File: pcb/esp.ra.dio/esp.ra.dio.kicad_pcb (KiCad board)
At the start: 2 copper layers, 75 x 28 mm, 24 parts, among them J1 A, J2 B, J3 C, J4 D, J5 START, J6 SELECT, J7 JOY, J8 BATTERY, J9 RADIO, SW1 OPTS, SW2 POWER, U1 RP2040 Tiny, U3 MIC5205-3.0YM5

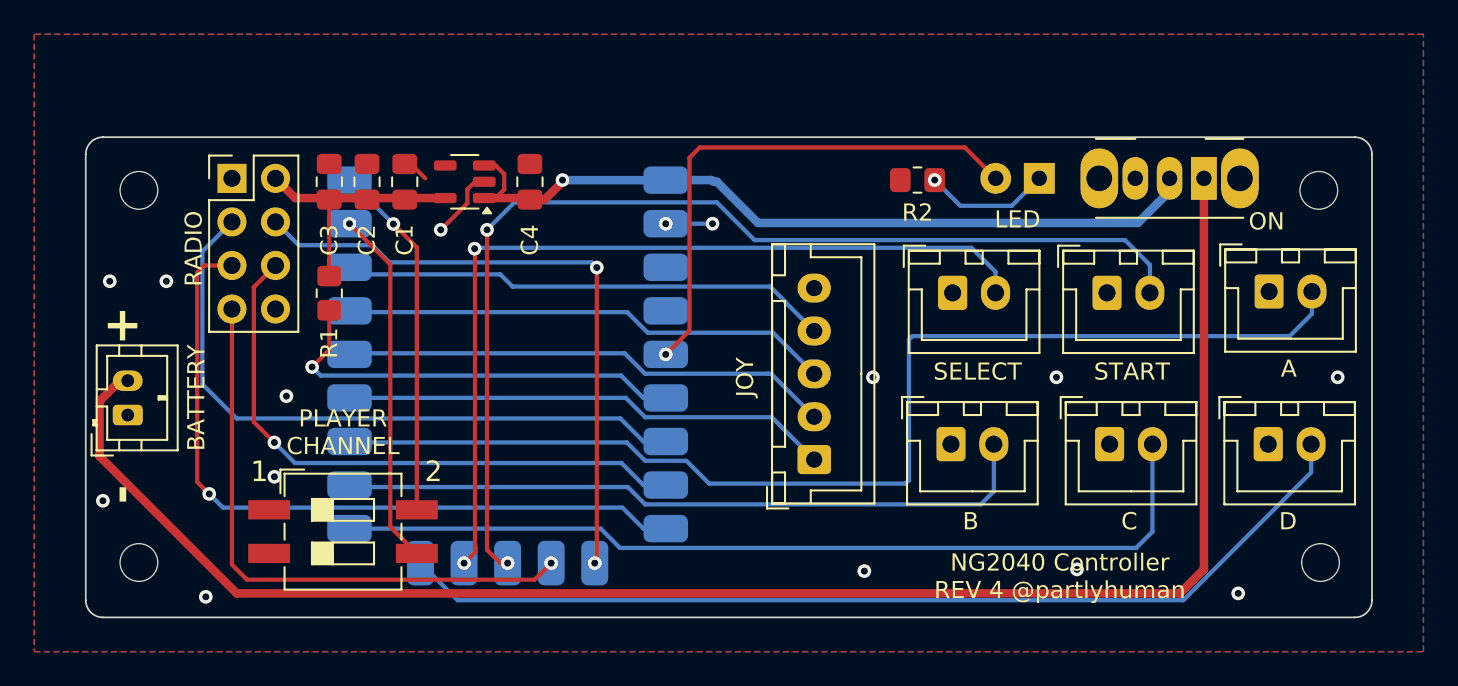
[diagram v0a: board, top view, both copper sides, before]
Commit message: super-mini symbol/footprint
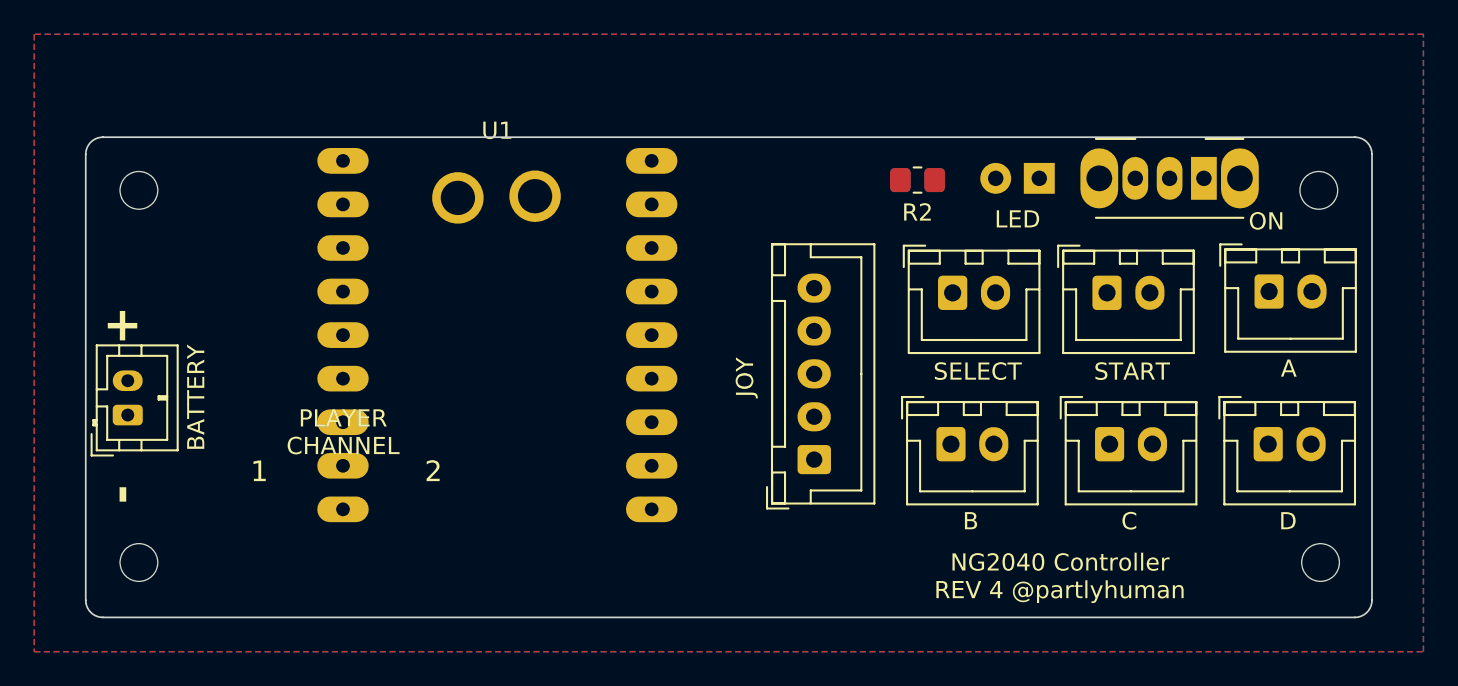
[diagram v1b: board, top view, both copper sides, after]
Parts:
- removed C1: 10uF, Capacitor_SMD:C_0805_2012Metric_Pad1.18x1.45mm_HandSolder
- removed C2: 0.1uF, Capacitor_SMD:C_0805_2012Metric_Pad1.18x1.45mm_HandSolder
- removed C3: 100nF, Capacitor_SMD:C_0805_2012Metric_Pad1.18x1.45mm_HandSolder
- removed C4: 1uF, Capacitor_SMD:C_0805_2012Metric_Pad1.18x1.45mm_HandSolder
- removed J9: RADIO, Connector_PinHeader_2.54mm:PinHeader_2x04_P2.54mm_Vertical
- removed R1: 10K, Resistor_SMD:R_0805_2012Metric_Pad1.20x1.40mm_HandSolder
- removed SW1: OPTS, Button_Switch_SMD:SW_DIP_SPSTx02_Slide_6.7x6.64mm_W8.61mm_P2.54mm_LowProfile
- removed U3: MIC5205-3.0YM5, Package_TO_SOT_SMD:SOT-23-5
- U1: value RP2040 Tiny -> ESP32-S3 Super Micro; footprint RP2040Zero:RP2040-Zero -> MCU_Espressif_ESP32_DevBoard:ESP32-S3-SuperMicro; moved to F.Cu
- moved U1 17.5 mm to (62.0, 61.5), turned to -90 degrees
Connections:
- SW2 pad 2: /VIN -> VCC
- U1 pad 1: /SET_PLAYER -> unconnected-(U1-TX-Pad1)
- U1 pad 10: /BD -> /D
- U1 pad 11: /SEL -> /C
- U1 pad 12: /STA -> /B
- U1 pad 13: /MISO -> /A
- U1 pad 14: /CS -> /STA
- U1 pad 15: /SCK -> /SEL
- U1 pad 16: /MOSI -> unconnected-(U1-3V3-Pad16)
- U1 pad 17: /CE -> GND
- U1 pad 18: Net-(U1-GP27) -> unconnected-(U1-5V-Pad18)
- U1 pad 19: /ACT_LED -> GND
- U1 pad 2: /SET_POWER -> unconnected-(U1-RX-Pad2)
- U1 pad 20: unconnected-(U1-GP29-Pad20) -> VCC
- U1 pad 3: /DL -> unconnected-(U1-GP1-Pad3)
- U1 pad 4: /DR -> unconnected-(U1-GP2-Pad4)
- U1 pad 5: /DD -> unconnected-(U1-GP3-Pad5)
- U1 pad 6: /DU -> /DL
- U1 pad 7: /BA -> /DR
- U1 pad 8: /BB -> /DD
- U1 pad 9: /BC -> /DU
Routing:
- net Net-(J8-Pin_2): track 96.4 -> 0.00 mm
- net /BA: track 67.3 -> 0.00 mm
- net /STA: track 62.6 -> 0.00 mm, vias 2 -> 0
- net /BD: track 57.6 -> 0.00 mm
- net /BC: track 52.8 -> 0.00 mm
- net /SEL: track 50.8 -> 0.00 mm, vias 2 -> 0
- net /VIN: track 46.7 -> 0.00 mm, vias 1 -> 0
- net /SCK: track 42.8 -> 0.00 mm, vias 1 -> 0
- net /BB: track 41.1 -> 0.00 mm
- net /CE: track 38.6 -> 0.00 mm
- net /CS: track 37.1 -> 0.00 mm, vias 2 -> 0
- net /MOSI: track 35.2 -> 0.00 mm, vias 1 -> 0
- net /MISO: track 34.3 -> 0.00 mm, vias 1 -> 0
- net /ACT_LED: track 30.9 -> 0.00 mm, vias 1 -> 0
- net /DD: track 28.7 -> 0.00 mm
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
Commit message: .
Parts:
- removed D1: LED, LED_THT:LED_D3.0mm_Horizontal_O1.27mm_Z6.0mm
- removed R2: 10K, Resistor_SMD:R_0805_2012Metric_Pad1.20x1.40mm_HandSolder
- removed SW2: POWER, Button_Switch_THT:SW_Slide_SPDT_Angled_CK_OS102011MA1Q
- J8: value BATTERY -> BAT
- U1: footprint MCU_Espressif_ESP32_DevBoard:ESP32-S3-SuperMicro -> MCU_Espressif_ESP32_DevBoard:ESP32-S3-SuperMicro_SMD_BATT
- moved U1 13.7 mm to (52.9, 51.2)
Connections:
- J8 pad 2: Net-(J8-Pin_2) -> /B+
- U1 pad 10: /D -> /BD
- U1 pad 11: /C -> /BC
- U1 pad 12: /B -> /BB
- U1 pad 13: /A -> /BA
- U1 pad 20: VCC -> /B+
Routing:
- net /BA: track 0.00 -> 55.0 mm
- net /BD: track 0.00 -> 43.9 mm
- net /BC: track 0.00 -> 36.5 mm
- net /STA: track 0.00 -> 32.9 mm, vias 0 -> 1
- net /DU: track 0.00 -> 32.6 mm, vias 0 -> 1
- net /B+: track 0.00 -> 30.8 mm
- net /DD: track 0.00 -> 29.8 mm, vias 0 -> 1
- net /DR: track 0.00 -> 28.7 mm, vias 0 -> 1
- net /DL: track 0.00 -> 28.7 mm, vias 0 -> 1
- net /BB: track 0.00 -> 27.6 mm
- net /SEL: track 0.00 -> 22.8 mm
- net GND: track 0.00 -> 3.11 mm, vias 0 -> 1
- removed copper zone on F.Cu, net GND
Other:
- board text removed: "1"
- board text removed: "2"
- board text removed: "ON"
- board text removed: "PLAYER CHANNEL"

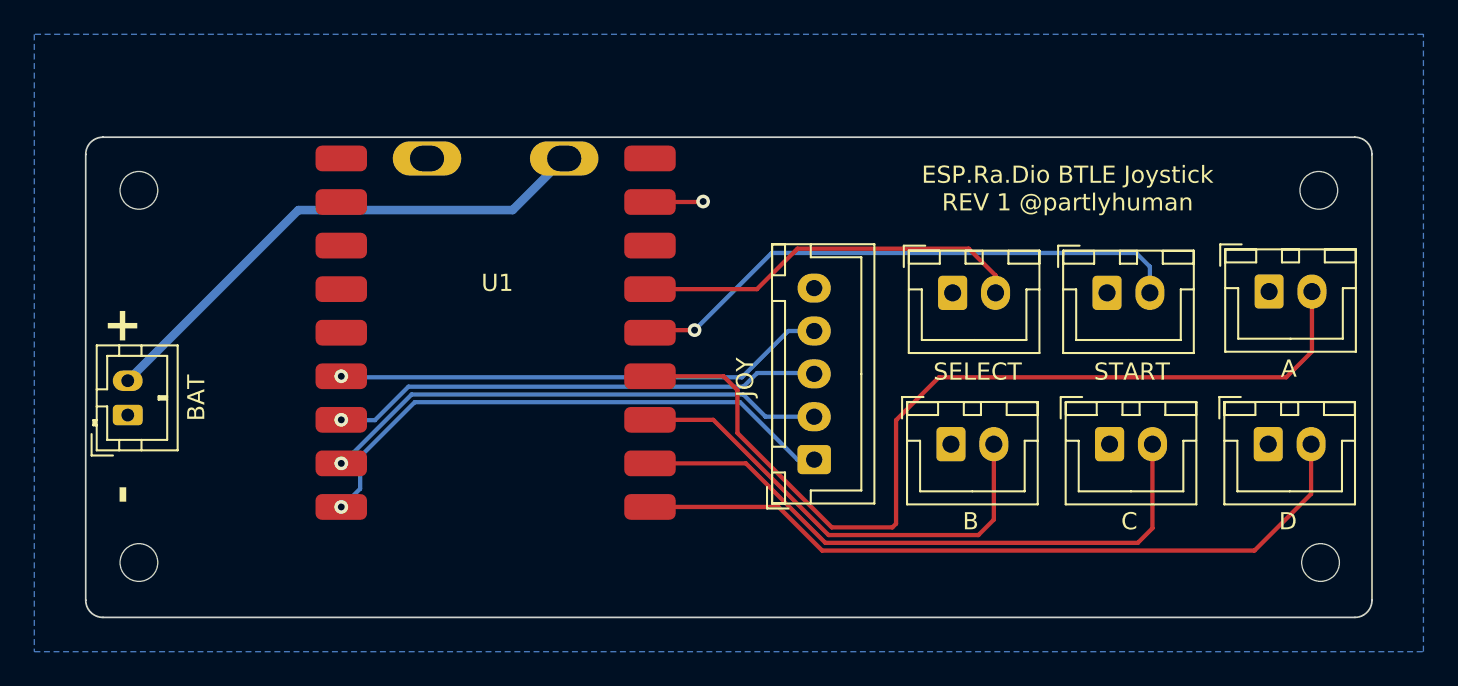
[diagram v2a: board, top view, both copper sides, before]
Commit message: Updated layout that keeps LED and switch
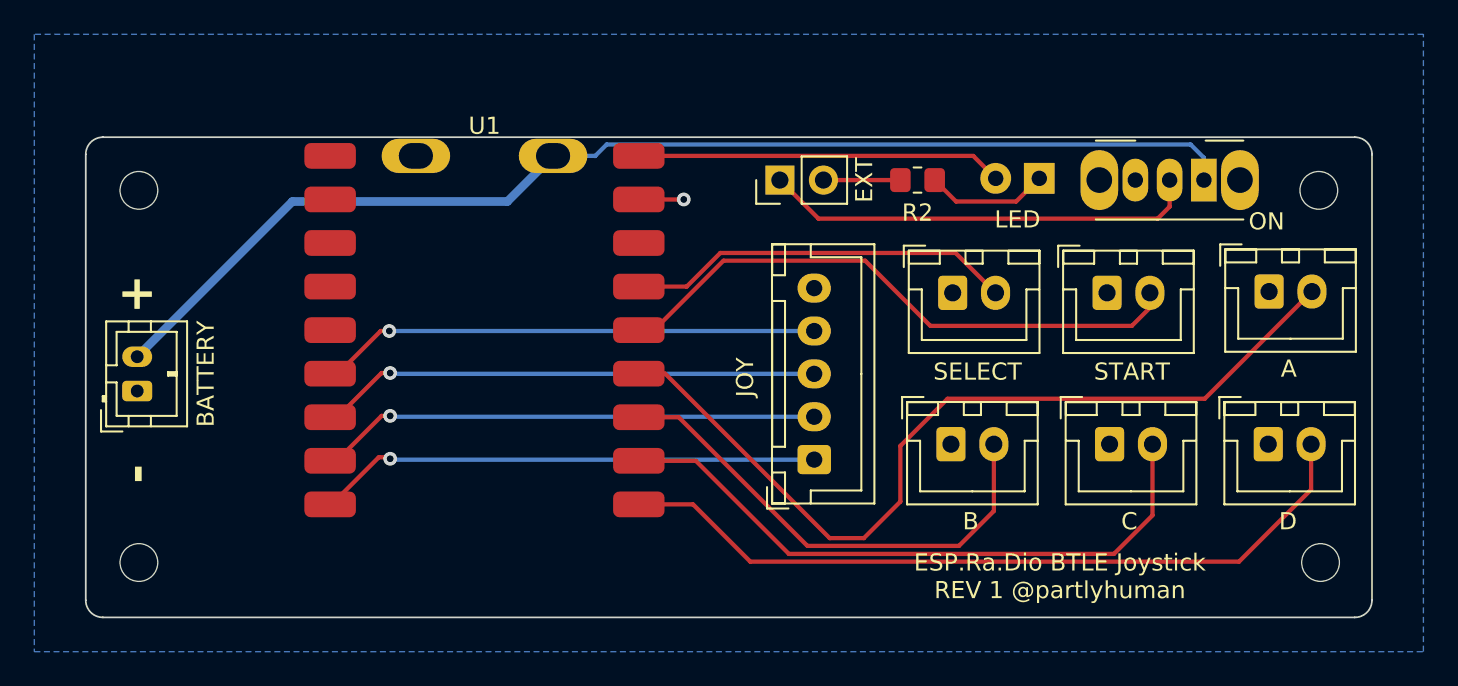
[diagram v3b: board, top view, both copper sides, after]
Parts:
- added D1: LED, LED_THT:LED_D3.0mm_Horizontal_O1.27mm_Z6.0mm, F.Cu at (93.6, 52.4)
- added J9: EXT, Connector_PinHeader_2.54mm:PinHeader_1x02_P2.54mm_Vertical, F.Cu at (78.5, 52.5)
- added R2: 10K, Resistor_SMD:R_0805_2012Metric_Pad1.20x1.40mm_HandSolder, F.Cu at (86.5, 52.5)
- added SW2: POWER, Button_Switch_THT:SW_Slide_SPDT_Angled_CK_OS102011MA1Q, F.Cu at (103.2, 52.5)
- J8: value BAT -> BATTERY
- moved J8 1.50 mm to (41.0, 64.8)
- moved U1 0.67 mm to (52.2, 51.1)
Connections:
- U1 pad 18: unconnected-(U1-5V-Pad18) -> /VBUS
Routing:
- net /B+: track 30.8 -> 69.2 mm
- net /LDO_CE: track 0.00 -> 25.5 mm
- net /VBUS: track 0.00 -> 21.4 mm
- net Net-(D1-K): track 0.00 -> 7.18 mm
- net /TP4054_CHRG: track 0.00 -> 4.48 mm
- net /BA: track 55.0 -> 51.1 mm
- net /DU: track 32.6 -> 29.4 mm
- net /STA: track 32.9 -> 34.4 mm, vias 1 -> 0
- net /BD: track 43.9 -> 45.0 mm
- net /BB: track 27.6 -> 28.5 mm
- net /BC: track 36.5 -> 37.3 mm
- net /DR: track 28.7 -> 29.3 mm
- net /DL: track 28.7 -> 29.3 mm
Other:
- board text added: "ON"

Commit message: Enough dev boards, redo with WROOM
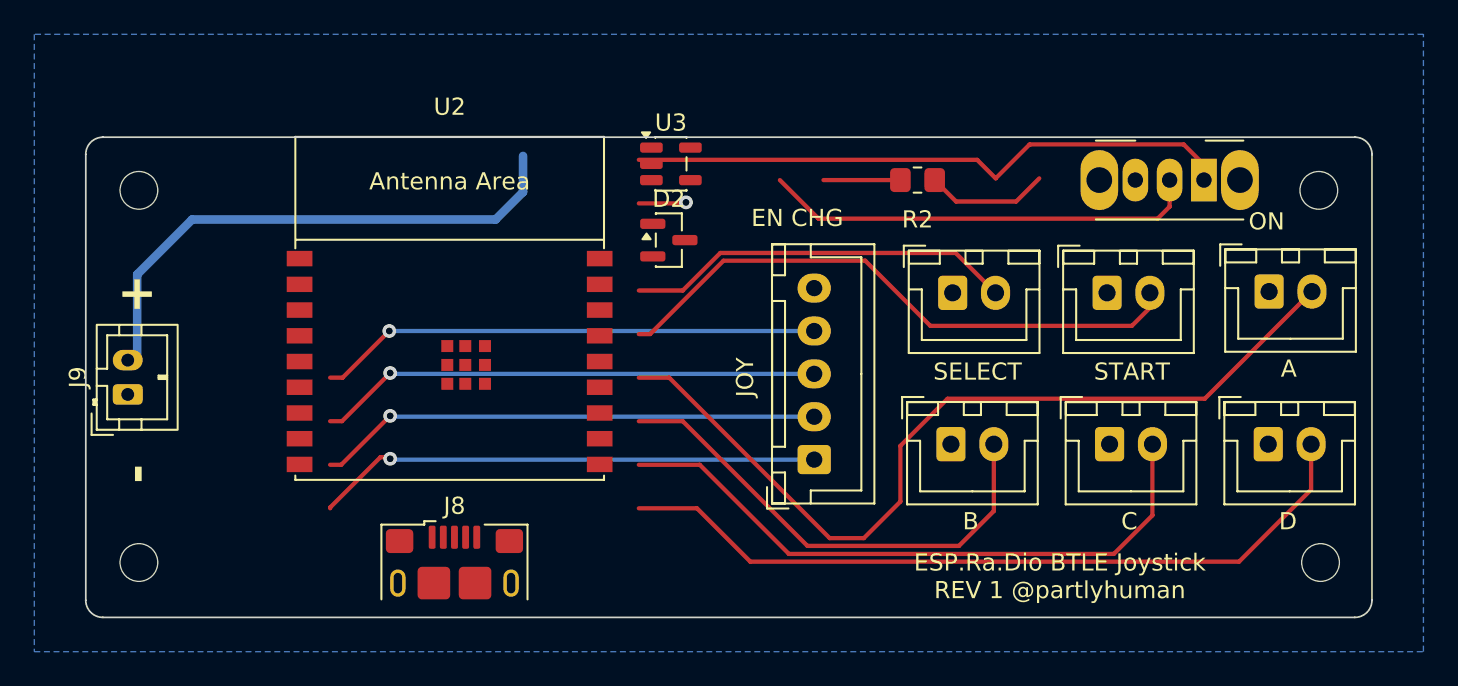
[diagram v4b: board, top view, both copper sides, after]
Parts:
- removed D1: LED, LED_THT:LED_D3.0mm_Horizontal_O1.27mm_Z6.0mm
- removed U1: ESP32-S3 Super Micro, MCU_Espressif_ESP32_DevBoard:ESP32-S3-SuperMicro_SMD_BATT
- added D2: BAT54C, Package_TO_SOT_SMD:SOT-23, F.Cu at (72.0, 56.0)
- added U2: ESP32-C3-WROOM-02, PCM_Espressif:ESP32-C3-WROOM-02, F.Cu at (59.2, 63.0)
- added U3: TLV75533PDBV, Package_TO_SOT_SMD:SOT-23-5, F.Cu at (72.1, 51.6)
- H1, H2, H3, H4: value MountingHole_2.2mm_M2 -> MountingHole
- J8: value BATTERY -> USB_B_Micro; footprint Connector_JST:JST_PH_B2B-PH-K_1x02_P2.00mm_Vertical -> Connector_USB:USB_Micro-B_Amphenol_10118193-0001LF_Horizontal
- J9: value EXT -> BATTERY; footprint Connector_PinHeader_2.54mm:PinHeader_1x02_P2.54mm_Vertical -> Connector_JST:JST_PH_B2B-PH-K_1x02_P2.00mm_Vertical
- R2: value 10K -> 0R
- moved J9 40.0 mm to (40.5, 65.0)
- moved J8 21.6 mm to (59.5, 76.0), turned to 0 degrees
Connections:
- J8 pad 1: GND -> /VBUS
- J8 pad 2: /B+ -> /USB_DN
- J9 pad 1: /LDO_CE -> GND
- J9 pad 2: /TP4054_CHRG -> /VBAT
- R2 pad 2: /TP4054_CHRG -> /USB_DP
- SW2 pad 1: /B+ -> GND
- SW2 pad 2: /LDO_CE -> Net-(SW2-B)
- SW2 pad 3: GND -> Net-(SW2-C)
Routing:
- net /B+: track 69.2 -> 0.00 mm
- net GND: track 2.62 -> 38.4 mm
- net /VBAT: track 0.00 -> 31.6 mm
- net Net-(SW2-B): track 0.00 -> 25.5 mm
- net /LDO_CE: track 25.5 -> 0.00 mm
- net /VBUS: track 21.4 -> 0.00 mm
- net /USB_DP: track 0.00 -> 4.48 mm
- net /TP4054_CHRG: track 4.48 -> 0.00 mm
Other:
- board text added: "EN CHG"

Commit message: Routing checkpoint
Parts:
- added C1: 10uF, Capacitor_SMD:C_0805_2012Metric_Pad1.18x1.45mm_HandSolder, F.Cu at (51.8, 61.0)
- added C2: 0.1uF, Capacitor_SMD:C_0805_2012Metric_Pad1.18x1.45mm_HandSolder, F.Cu at (54.2, 61.0)
- added C3: 1uF, Capacitor_SMD:C_0805_2012Metric_Pad1.18x1.45mm_HandSolder, F.Cu at (58.5, 74.5)
- added J10: UART, Connector_PinHeader_2.54mm:PinHeader_1x04_P2.54mm_Vertical, F.Cu at (80.0, 53.0)
- added R1: 0R, Resistor_SMD:R_0805_2012Metric_Pad1.20x1.40mm_HandSolder, F.Cu at (54.2, 66.0)
- added R3: 10K, Resistor_SMD:R_0805_2012Metric_Pad1.20x1.40mm_HandSolder, F.Cu at (61.5, 74.5)
- added SW1: RESET, Button_Switch_SMD:SW_SPST_PTS810, F.Cu at (67.0, 74.5)
- added SW3: BOOT, Button_Switch_SMD:SW_SPST_PTS810, F.Cu at (73.5, 74.5)
- J8: footprint Connector_USB:USB_Micro-B_Amphenol_10118193-0001LF_Horizontal -> Connector_USB:USB_Micro-AB_Molex_47590-0001
- moved SW2 50.7 mm to (52.5, 52.5)
- moved R2 37.3 mm to (51.8, 66.0), turned to -90 degrees
- moved U3 28.8 mm to (47.2, 66.0), turned to -90 degrees
- moved D2 25.2 mm to (47.2, 61.0), turned to 90 degrees
- moved J8 8.80 mm to (50.8, 76.9)
- moved U2 7.30 mm to (66.5, 63.5)
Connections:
- net Net-(SW2-B) renamed /VIN
- net Net-(SW2-C) renamed /VBATBUS
- D2 pad 1: /VBUS -> /VBAT
- D2 pad 2: /VBAT -> /VBUS
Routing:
- net /BA: track 51.0 -> 0.00 mm
- net /BD: track 44.9 -> 0.00 mm
- net /BC: track 37.2 -> 0.00 mm
- net /STA: track 34.5 -> 0.00 mm
- net GND: track 38.4 -> 4.27 mm, vias 1 -> 0
- net /DU: track 29.5 -> 0.00 mm, vias 1 -> 0
- net /DD: track 29.4 -> 0.00 mm, vias 1 -> 0
- net /DR: track 29.4 -> 0.00 mm, vias 1 -> 0
- net /DL: track 29.4 -> 0.00 mm, vias 1 -> 0
- net /BB: track 28.5 -> 0.00 mm
- net /VBAT: track 31.6 -> 6.24 mm
- net Net-(U2-GPIO9): track 0.00 -> 24.1 mm
- net /SEL: track 22.7 -> 0.00 mm
- net Net-(U2-GPIO18/USB_D-): track 0.00 -> 21.0 mm, vias 0 -> 2
- net Net-(U2-EN/CHIP_PU): track 0.00 -> 20.2 mm
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- added copper zone on F.Cu, net GND
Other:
- outline, holes or cut-outs redrawn

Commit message: Routing checkpoint
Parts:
- moved J10 22.9 mm to (87.7, 74.6), turned to -90 degrees
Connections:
- U2 pad 10: /BD -> /BC
- U2 pad 7: /BC -> /BD
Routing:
- net /BD: track 0.00 -> 55.3 mm
- net /BA: track 0.00 -> 38.1 mm
- net /DU: track 0.00 -> 27.4 mm, vias 0 -> 1
- net /BC: track 0.00 -> 27.0 mm
- net /STA: track 0.00 -> 26.7 mm
- net /DD: track 0.00 -> 26.1 mm, vias 0 -> 1
- net /DR: track 0.00 -> 24.8 mm, vias 0 -> 1
- net /BB: track 0.00 -> 24.4 mm
- net /DL: track 0.00 -> 23.5 mm, vias 0 -> 1
- net /SEL: track 0.00 -> 17.9 mm
- net /TXD: track 0.00 -> 13.7 mm, vias 0 -> 1
- net /RXD: track 0.00 -> 10.3 mm, vias 0 -> 1
- net GND: vias 0 -> 16
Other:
- board text added: "- +"
- board text added: "OFF"
- board text removed: "+"
- board text removed: "-"
- board text removed: "EN CHG"
